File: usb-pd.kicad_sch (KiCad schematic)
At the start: 71 parts, among them J3 USB-C_GCT_USB4105-GF-A, J4 JST_SH_1x4_SM04B-SRSS-TB-LF-SN, Q4 SQS401EN-T1_BE3, U2 TVS2200DRVR, U6 STUSB4500_QFN, U9 SIC477ED-T1-GE3

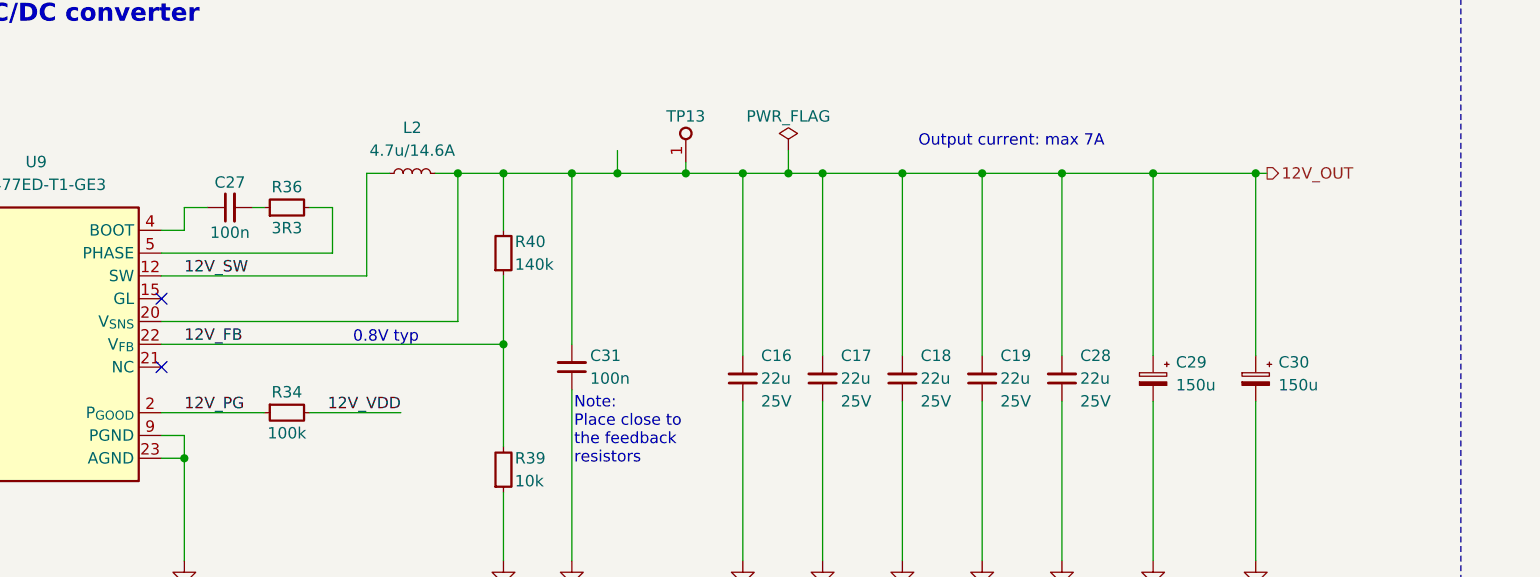
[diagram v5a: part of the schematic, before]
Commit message: [#79262] Remove 12V DC-DC R_boot resistor
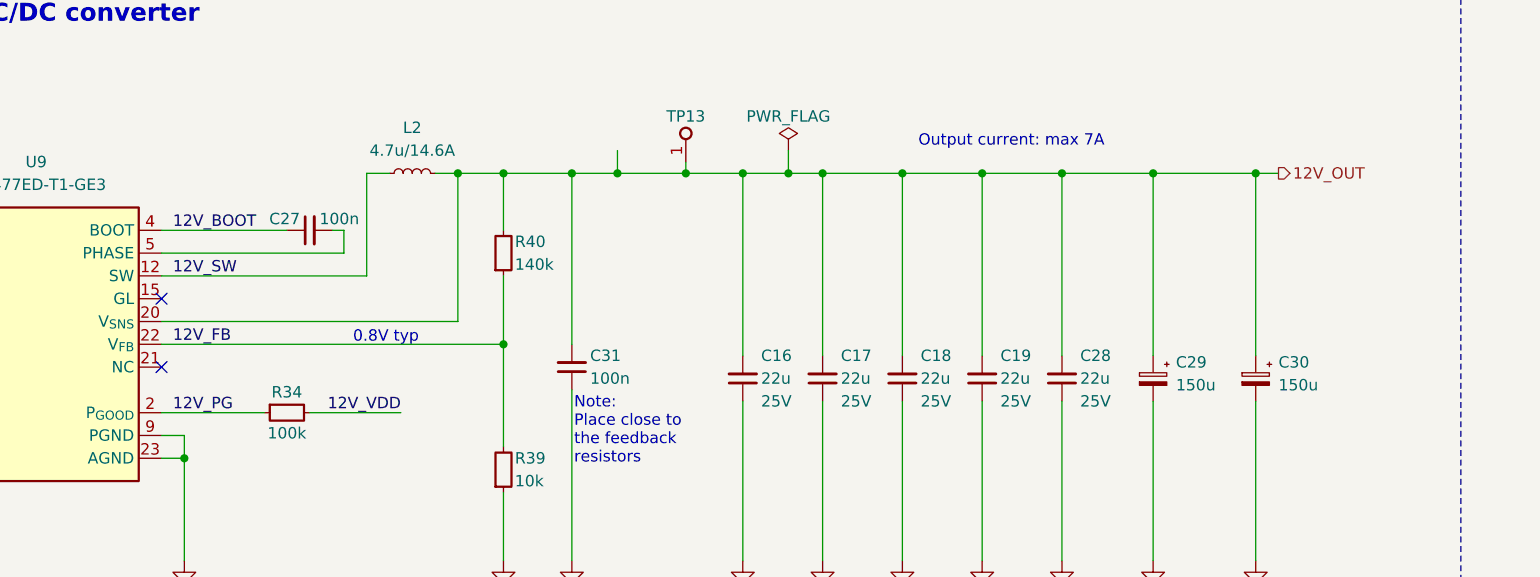
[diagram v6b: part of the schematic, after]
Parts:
- removed R36: R_3R3_0402, antmicro-footprints:R_0402_1005Metric, symbol antmicroResistors0402:R_3R3_0402
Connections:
- net 12V_BOOT: now reaches C27.1, U9.4 (BOOT)
- net at C27.2: now also U9.5 (PHASE), U9.6 (PHASE)
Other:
- moved on the sheet: C27
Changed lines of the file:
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@@
 	(wire
 		(pts
-			(xy 144.78 203.2) (xy 163.83 203.2)
+			(xy 144.78 203.2) (xy 165.1 203.2)
 		)
 		(stroke
@@
 	(wire
 		(pts
-			(xy 147.32 198.12) (xy 147.32 200.66)
-		)
-		(stroke
-			(width 0)
-			(type default)
-		)
-	)
-	(wire
-		(pts
 			(xy 233.68 107.95) (xy 233.68 111.76)
 		)
@@
 		)
 	)
+	(wire
+		(pts
+			(xy 165.1 200.66) (xy 163.83 200.66)
+		)
+		(stroke
+			(width 0)
+			(type default)
+		)
+	)
 	(polyline
 		(pts
@@
 	(wire
 		(pts
-			(xy 163.83 198.12) (xy 161.29 198.12)
-		)
-		(stroke
-			(width 0)
-			(type default)
-		)
-	)
-	(wire
-		(pts
 			(xy 233.68 99.06) (xy 233.68 102.87)
 		)
@@
 	(wire
 		(pts
-			(xy 163.83 203.2) (xy 163.83 198.12)
+			(xy 165.1 203.2) (xy 165.1 200.66)
 		)
 		(stroke
@@
 	(wire
 		(pts
-			(xy 154.94 198.12) (xy 156.21 198.12)
-		)
-		(stroke
-			(width 0)
-			(type default)
-		)
-	)
-	(wire
-		(pts
 			(xy 74.93 201.93) (xy 74.93 203.2)
 		)
@@
 	(wire
 		(pts
-			(xy 147.32 198.12) (xy 149.86 198.12)
-		)
-		(stroke
-			(width 0)
-			(type default)
-		)
-	)
-	(wire
-		(pts
 			(xy 190.5 194.31) (xy 190.5 213.36)
 		)
@@
 	(wire
 		(pts
-			(xy 144.78 200.66) (xy 147.32 200.66)
+			(xy 144.78 200.66) (xy 158.75 200.66)
 		)
 		(stroke
@@
 	(wire
 		(pts
-			(xy 267.97 194.31) (xy 266.7 194.31)
+			(xy 269.24 194.31) (xy 266.7 194.31)
 		)
 		(stroke
@@
 	)
 	(label "12V_SW"
-		(at 147.32 205.74 0)
+		(at 146.05 205.74 0)
 		(effects
 			(font
@@
 		)
 	)
+	(label "12V_BOOT"
+		(at 146.05 200.66 0)
+		(effects
+			(font
+				(size 1.27 1.27)
+			)
+			(justify left bottom)
+		)
+	)
 	(label "SCL"
 		(at 393.7 88.9 180)
@@
 	)
 	(label "12V_FB"
-		(at 147.32 213.36 0)
+		(at 146.05 213.36 0)
 		(effects
 			(font
@@
 	)
 	(label "12V_PG"
-		(at 147.32 220.98 0)
+		(at 146.05 220.98 0)
 		(effects
 			(font
@@
 	(hierarchical_label "12V_OUT"
 		(shape output)
-		(at 267.97 194.31 0)
+		(at 269.24 194.31 0)
 		(effects
 			(font
@@
 	(symbol
 		(lib_id "antmicroCapacitors0402:C_100n_0402")
-		(at 149.86 198.12 0)
+		(at 158.75 200.66 0)
 		(unit 1)
 		(exclude_from_sim no)
@@
 		(dnp no)
 		(property "Reference" "C27"
-			(at 152.4 195.326 0)
+			(at 158.496 199.39 0)
 			(effects
 				(font
@@
 		)
 		(property "Value" "C_100n_0402"
-			(at 170.18 208.28 0)
+			(at 179.07 210.82 0)
 			(effects
 				(font
@@
 		)
 		(property "Footprint" "antmicro-footprints:C_0402_1005Metric"
-			(at 170.18 210.82 0)
+			(at 179.07 213.36 0)
 			(effects
 				(font
@@
 		)
 		(property "Datasheet" "https://www.murata.com/products/productdetail?partno=GRM155R61H104KE14%23"
-			(at 170.18 213.36 0)
+			(at 179.07 215.9 0)
 			(effects
 				(font
@@
 		)
 		(property "Description" "SMD Multilayer Ceramic Capacitor, 0.1 µF, 50 V, 0402 [1005 Metric], ± 10%, X5R, GRM Series"
-			(at 149.86 198.12 0)
+			(at 158.75 200.66 0)
 			(effects
 				(font
@@
 		)
 		(property "MPN" "GRM155R61H104KE14D"
-			(at 170.18 215.9 0)
+			(at 179.07 218.44 0)
 			(effects
 				(font
@@
 		)
 		(property "Manufacturer" "Murata"
-			(at 170.18 218.44 0)
+			(at 179.07 220.98 0)
 			(effects
 				(font
@@
 		)
 		(property "License" "Apache-2.0"
-			(at 170.18 220.98 0)
+			(at 179.07 223.52 0)
 			(effects
 				(font
@@
 		)
 		(property "Author" "Antmicro"
-			(at 170.18 223.52 0)
+			(at 179.07 226.06 0)
 			(effects
 				(font
@@
 		)
 		(property "Val" "100n"
-			(at 152.4 200.914 0)
+			(at 164.592 199.39 0)
 			(effects
 				(font
@@
 		)
 		(property "Voltage" "50V"
-			(at 170.18 226.06 0)
+			(at 179.07 228.6 0)
 			(effects
 				(font
@@
 		)
 		(property "Dielectric" "X5R"
-			(at 170.18 228.6 0)
+			(at 179.07 231.14 0)
 			(effects
 				(font
@@
 					(unit 1)
 				)
-			)
-		)
-	)
-	(symbol
-		(lib_id "antmicroResistors0402:R_3R3_0402")
-		(at 156.21 198.12 0)
-		(mirror x)
-		(unit 1)
-		(exclude_from_sim no)
-		(in_bom yes)
-		(on_board yes)
-		(dnp no)
-		(property "Reference" "R36"
-			(at 158.75 195.834 0)
-			(effects
-				(font
-					(size 1.27 1.27)
-				)
-			)
-		)
-		(property "Value" "R_3R3_0402"
-			(at 156.21 194.31 0)
-			(effects
-				(font
-					(size 1.27 1.27)
-				)
-				(justify left)
-				(hide yes)
-			)
-		)
-		(property "Footprint" "antmicro-footprints:R_0402_1005Metric"
-			(at 161.29 203.2 0)
-			(effects
-				(font
-					(size 1.27 1.27)
-					(thickness 0.15)
-				)
-				(justify left bottom)
-				(hide yes)
-			)
-		)
-		(property "Datasheet" "https://www.bourns.com/docs/product-datasheets/cr.pdf"
-			(at 156.21 198.12 0)
-			(effects
-				(font
-					(size 1.27 1.27)
-					(thickness 0.15)
-				)
-				(justify left bottom)
-				(hide yes)
-			)
-		)
-		(property "Description" "SMD Chip Resistor, 3.3 ohm, ± 1%, 62.5 mW, 0402 [1005 Metric], Thick Film, General Purpose"
-			(at 156.21 198.12 0)
-			(effects
-				(font
-					(size 1.27 1.27)
-				)
-				(hide yes)
-			)
-		)
-		(property "Manufacturer" "Bourns"
-			(at 161.29 208.28 0)
-			(effects
-				(font
-					(size 1.27 1.27)
-					(thickness 0.15)
-				)
-				(justify left bottom)
-				(hide yes)
-			)
-		)
-		(property "MPN" "CR0402-FX-3R30GLF"
-			(at 161.29 205.74 0)
-			(effects
-				(font
-					(size 1.27 1.27)
-					(thickness 0.15)
-				)
-				(justify left bottom)
-				(hide yes)
-			)
-		)
-		(property "Val" "3R3"
-			(at 158.75 200.406 0)
-			(effects
-				(font
-					(size 1.27 1.27)
-					(thickness 0.15)
-				)
-			)
-		)
-		(property "License" "Apache-2.0"
-			(at 176.53 172.72 0)
-			(effects
-				(font
-					(size 1.27 1.27)
-					(thickness 0.15)
-				)
-				(justify left bottom)
-				(hide yes)
-			)
-		)
-		(property "Author" "Antmicro"
-			(at 176.53 170.18 0)
-			(effects
-				(font
-					(size 1.27 1.27)
-					(thickness 0.15)
-				)
-				(justify left bottom)
-				(hide yes)
-			)
-		)
-		(property "Tolerance" "1%"
-			(at 176.53 187.96 0)
-			(effects
-				(font
-					(size 1.27 1.27)
-				)
-				(justify left bottom)
-				(hide yes)
-			)
-		)
-		(pin "1"
-		)
-		(pin "2"
-		)
-		(instances
-			(project "oculink-to-pcie-adapter"
-				(path "/44c3be85-0a18-4d93-a9a5-650ee09b6032/967dc2ce-6faa-4f65-adf2-eb5d333aef74"
-					(reference "R36")
-					(unit 1)
-				)

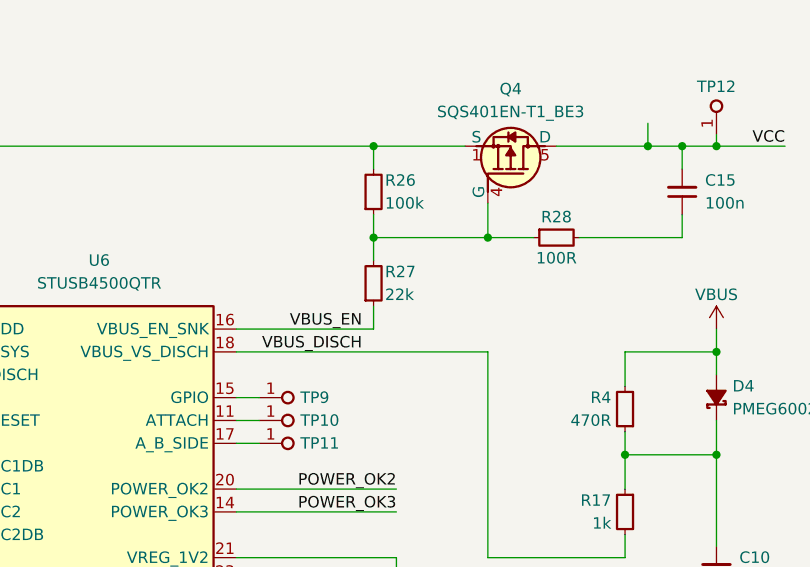
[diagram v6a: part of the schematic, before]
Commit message: [#79262] Reduce Q4 max Vgs
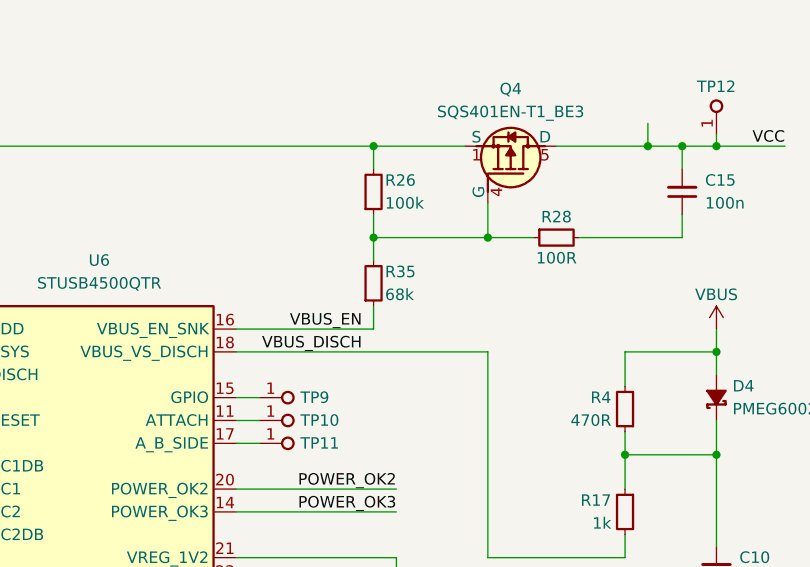
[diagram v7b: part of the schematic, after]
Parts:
- removed R27: R_22k_0402, antmicro-footprints:R_0402_1005Metric, symbol antmicroResistors0402:R_22k_0402
- added R35: R_68k_0402, antmicro-footprints:R_0402_1005Metric, symbol antmicroResistors0402:R_68k_0402
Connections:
- net VBUS_EN: now also R35.1
- net at Q4.4 (G), R26.1, R28.1: now also R35.2
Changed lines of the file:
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@@
 	)
 	(symbol
+		(lib_id "antmicroResistors0402:R_68k_0402")
+		(at 240.03 68.58 90)
+		(unit 1)
+		(exclude_from_sim no)
+		(in_bom yes)
+		(on_board yes)
+		(dnp no)
+		(property "Reference" "R35"
+			(at 241.3 64.77 90)
+			(effects
+				(font
+					(size 1.27 1.27)
+					(thickness 0.15)
+				)
+				(justify right)
+			)
+		)
+		(property "Value" "R_68k_0402"
+			(at 252.73 48.26 0)
+			(effects
+				(font
+					(size 1.27 1.27)
+					(thickness 0.15)
+				)
+				(justify left bottom)
+				(hide yes)
+			)
+		)
+		(property "Footprint" "antmicro-footprints:R_0402_1005Metric"
+			(at 255.27 48.26 0)
+			(effects
+				(font
+					(size 1.27 1.27)
+					(thickness 0.15)
+				)
+				(justify left bottom)
+				(hide yes)
+			)
+		)
+		(property "Datasheet" "https://www.bourns.com/docs/product-datasheets/cr.pdf"
+			(at 257.81 48.26 0)
+			(effects
+				(font
+					(size 1.27 1.27)
+					(thickness 0.15)
+				)
+				(justify left bottom)
+				(hide yes)
+			)
+		)
+		(property "Description" "SMD Chip Resistor"
+			(at 240.03 68.58 0)
+			(effects
+				(font
+					(size 1.27 1.27)
+				)
+				(hide yes)
+			)
+		)
+		(property "MPN" "CR0402-FX-6802GLF"
+			(at 260.35 48.26 0)
+			(effects
+				(font
+					(size 1.27 1.27)
+					(thickness 0.15)
+				)
+				(justify left bottom)
+				(hide yes)
+			)
+		)
+		(property "Manufacturer" "Bourns"
+			(at 262.89 48.26 0)
+			(effects
+				(font
+					(size 1.27 1.27)
+					(thickness 0.15)
+				)
+				(justify left bottom)
+				(hide yes)
+			)
+		)
+		(property "License" "Apache-2.0"
+			(at 265.43 48.26 0)
+			(effects
+				(font
+					(size 1.27 1.27)
+					(thickness 0.15)
+				)
+				(justify left bottom)
+				(hide yes)
+			)
+		)
+		(property "Author" "Antmicro"
+			(at 267.97 48.26 0)
+			(effects
+				(font
+					(size 1.27 1.27)
+					(thickness 0.15)
+				)
+				(justify left bottom)
+				(hide yes)
+			)
+		)
+		(property "Val" "68k"
+			(at 241.3 67.31 90)
+			(effects
+				(font
+					(size 1.27 1.27)
+					(thickness 0.15)
+				)
+				(justify right)
+			)
+		)
+		(property "Tolerance" "1%"
+			(at 250.19 48.26 0)
+			(effects
+				(font
+					(size 1.27 1.27)
+				)
+				(justify left bottom)
+				(hide yes)
+			)
+		)
+		(pin "2"
+		)
+		(pin "1"
+		)
+		(instances
+			(project ""
+				(path "/44c3be85-0a18-4d93-a9a5-650ee09b6032/967dc2ce-6faa-4f65-adf2-eb5d333aef74"
+					(reference "R35")
+					(unit 1)
+				)
+			)
+		)
+	)
+	(symbol
 		(lib_id "antmicroPMICPowerDistributionSwitchesLoadDrivers:STUSB4500_QFN")
 		(at 194.31 71.12 0)
@@
 					(unit 1)
 				)
-			)
-		)
-	)
-	(symbol
-		(lib_id "antmicroResistors0402:R_22k_0402")
-		(at 240.03 68.58 90)
-		(unit 1)
-		(exclude_from_sim no)
-		(in_bom yes)
-		(on_board yes)
-		(dnp no)
-		(property "Reference" "R27"
-			(at 241.3 64.77 90)
-			(effects
-				(font
-					(size 1.27 1.27)
-					(thickness 0.15)
-				)
-				(justify right)
-			)
-		)
-		(property "Value" "R_22k_0402"
-			(at 252.73 48.26 0)
-			(effects
-				(font
-					(size 1.27 1.27)
-					(thickness 0.15)
-				)
-				(justify left bottom)
-				(hide yes)
-			)
-		)
-		(property "Footprint" "antmicro-footprints:R_0402_1005Metric"
-			(at 255.27 48.26 0)
-			(effects
-				(font
-					(size 1.27 1.27)
-					(thickness 0.15)
-				)
-				(justify left bottom)
-				(hide yes)
-			)
-		)
-		(property "Datasheet" "https://www.bourns.com/docs/product-datasheets/cr.pdf"
-			(at 257.81 48.26 0)
-			(effects
-				(font
-					(size 1.27 1.27)
-					(thickness 0.15)
-				)
-				(justify left bottom)
-				(hide yes)
-			)
-		)
-		(property "Description" "SMD Chip Resistor, 22 kohm, ± 1%, 62.5 mW, 0402 [1005 Metric], Thick Film, General Purpose"
-			(at 240.03 68.58 0)
-			(effects
-				(font
-					(size 1.27 1.27)
-				)
-				(hide yes)
-			)
-		)
-		(property "MPN" "CR0402-FX-2202GLF"
-			(at 260.35 48.26 0)
-			(effects
-				(font
-					(size 1.27 1.27)
-					(thickness 0.15)
-				)
-				(justify left bottom)
-				(hide yes)
-			)
-		)
-		(property "Manufacturer" "Bourns"
-			(at 262.89 48.26 0)
-			(effects
-				(font
-					(size 1.27 1.27)
-					(thickness 0.15)
-				)
-				(justify left bottom)
-				(hide yes)
-			)
-		)
-		(property "License" "Apache-2.0"
-			(at 265.43 48.26 0)
-			(effects
-				(font
-					(size 1.27 1.27)
-					(thickness 0.15)
-				)
-				(justify left bottom)
-				(hide yes)
-			)
-		)
-		(property "Author" "Antmicro"
-			(at 267.97 48.26 0)
-			(effects
-				(font
-					(size 1.27 1.27)
-					(thickness 0.15)
-				)
-				(justify left bottom)
-				(hide yes)
-			)
-		)
-		(property "Val" "22k"
-			(at 241.3 67.31 90)
-			(effects
-				(font
-					(size 1.27 1.27)
-					(thickness 0.15)
-				)
-				(justify right)
-			)
-		)
-		(property "Tolerance" "1%"
-			(at 250.19 48.26 0)
-			(effects
-				(font
-					(size 1.27 1.27)
-				)
-				(justify left bottom)
-				(hide yes)
-			)
-		)
-		(pin "1"
-		)
-		(pin "2"
-		)
-		(instances
-			(project "oculink-to-pcie-adapter"
-				(path "/44c3be85-0a18-4d93-a9a5-650ee09b6032/967dc2ce-6faa-4f65-adf2-eb5d333aef74"
-					(reference "R27")
-					(unit 1)
-				)

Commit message: [#79262] Change USB PD controller to CYPD3177
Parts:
- removed C10: C_10u_0805_35V, antmicro-footprints:C_0805_2012Metric, symbol antmicroCapacitorsmisc:C_10u_0805_35V
- removed C11, C15: C_100n_0402, antmicro-footprints:C_0402_1005Metric, symbol antmicroCapacitors0402:C_100n_0402
- removed C12, C13, C14: C_1u_25V_0402, antmicro-footprints:C_0402_1005Metric, symbol antmicroCapacitors0402:C_1u_25V_0402
- removed D18: ESD204DQAR, antmicro-footprints:USON-10_2.5x1mm_P0.5mm, symbol antmicroTVSDiodes:ESD204DQAR
- removed D4: PMEG6002EJ,115, antmicro-footprints:D_SOD-323F, symbol antmicroDiodesRectifiersSingle:PMEG6002EJ,115
- removed D6, D7: LED_G_0603_LTST-C190GKT, antmicro-footprints:LED_0603_1608Metric_G, symbol antmicroLEDIndicationDiscrete:LED_G_0603_LTST-C190GKT
- removed J4: JST_SH_1x4_SM04B-SRSS-TB-LF-SN, antmicro-footprints:Conn_JST_SH_1x4_SM04B-SRSS-TB-LF-SN, symbol antmicroWire2BoardConnectors:JST_SH_1x4_SM04B-SRSS-TB-LF-SN
- removed Q4: SQS401EN-T1_BE3, antmicro-footprints:Vishay_PowerPAK_1212-8_Single, symbol antmicroTransistorsFETsMOSFETsSingle:SQS401EN-T1_BE3
- removed R17, R24, R25: R_1k_0402, antmicro-footprints:R_0402_1005Metric, symbol antmicroResistors0402:R_1k_0402
- removed R18: R_0R_0402, antmicro-footprints:R_0402_1005Metric, symbol antmicroResistors0402:R_0R_0402
- removed R19, R20, R22: R_4k7_0402, antmicro-footprints:R_0402_1005Metric, symbol antmicroResistors0402:R_4k7_0402
- removed R26: R_100k_0402, antmicro-footprints:R_0402_1005Metric, symbol antmicroResistors0402:R_100k_0402
- removed R28: R_100R_0402, antmicro-footprints:R_0402_1005Metric, symbol antmicroResistors0402:R_100R_0402
- removed R35: R_68k_0402, antmicro-footprints:R_0402_1005Metric, symbol antmicroResistors0402:R_68k_0402
- removed R4: R_470R_0402, antmicro-footprints:R_0402_1005Metric, symbol antmicroResistors0402:R_470R_0402
- removed TP10, TP11, TP12, TP7, TP8, TP9: TP_0.75mm_SMD, antmicro-footprints:TP_SMD_0.75mm, symbol antmicroTestPoints:TP_0.75mm_SMD
- removed U2: TVS2200DRVR, antmicro-footprints:WSON-6-1EP_2x2mm_P0.65mm, symbol antmicroTVSDiodes:TVS2200DRVR
- removed U6: STUSB4500_QFN, antmicro-footprints:QFN-24-1EP_4x4mm_P0.5_EP2.1x2.1mm, symbol antmicroPMICPowerDistributionSwitchesLoadDrivers:STUSB4500_QFN
- added C11, C38, C39: C_1u_25V_0402, antmicro-footprints:C_0402_1005Metric, symbol antmicroCapacitors0402:C_1u_25V_0402
- added C40, C41: C_100n_0402, antmicro-footprints:C_0402_1005Metric, symbol antmicroCapacitors0402:C_100n_0402
- added D18: LED_G_0603_LTST-C190GKT, antmicro-footprints:LED_0603_1608Metric_G, symbol antmicroLEDIndicationDiscrete:LED_G_0603_LTST-C190GKT
- added D19: BZT52B15SV-T, antmicro-footprints:D_SOD-323, symbol antmicroDiodesZenerSingle:BZT52B15SV-T
- added D21: ESDA25P35-1U1M, antmicro-footprints:QFN-2L_1.6x1x0.55mm, symbol antmicroTVSDiodes:ESDA25P35-1U1M
- added Q6: SQS401EN-T1_BE3, antmicro-footprints:Vishay_PowerPAK_1212-8_Single, symbol antmicroTransistorsFETsMOSFETsSingle:SQS401EN-T1_BE3
- added Q8: BSS138-7-F, antmicro-footprints:SOT-23-3, symbol antmicroTransistorsFETsMOSFETsSingle:BSS138-7-F
- added R17, R22, R24, R25, R26, R27, R28, R38, R4, R41: R_10k_0402, antmicro-footprints:R_0402_1005Metric, symbol antmicroResistors0402:R_10k_0402
- added R18, R19: R_2k_0402, antmicro-footprints:R_0402_1005Metric, symbol antmicroResistors0402:R_2k_0402
- added R20: R_49k9_0402, antmicro-footprints:R_0402_1005Metric, symbol antmicroResistors0402:R_49k9_0402
- added R37: R_1k_0402, antmicro-footprints:R_0402_1005Metric, symbol antmicroResistors0402:R_1k_0402
- added TP14: TP_0.75mm_SMD, antmicro-footprints:TP_SMD_0.75mm, symbol antmicroTestPoints:TP_0.75mm_SMD
- added U5: CYPD3177-24LQXQ, antmicro-footprints:QFN-24-1EP_4x4mm_P0.5mm_EP2.6x2.6mm, symbol antmicroInterfaceControllers:CYPD3177-24LQXQ
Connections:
- net CC1: now also U5.15 (CC1)
- net CC2: now also U5.14 (CC2)
- net GND: now also C11.1, C39.1, C40.1, C41.1, D21.2 (A), Q8.2 (S), R17.1, R22.1, R25.1, R28.1, R38.1, U5.19 (GND), U5.22 (GND), U5.25 (GND); no longer R21.2
- net SCL: now also R18.1, U5.13 (HPI_SCL); no longer TP6.1
- net SDA: now also R19.1, U5.12 (HPI_SDA); no longer TP5.1
- net VBUS: now also D19.1 (C), D21.1 (C), Q6.1 (S), Q6.2 (S), Q6.3 (S), R27.2, R41.2, U5.18 (VBUS_IN)
- net VBUS_EN: now also R37.1, U5.3 (VBUS_FET_EN)
- net VCC: now also C38.2, Q6.5 (D), TP14.1, U5.11 (VDC_OUT)
- net VBUS_MAX: now reaches R21.1
- net VBUS_MAX: now also R22.2, U5.2 (VBUS_MAX)
- new net: C38.1, D19.2 (A), Q6.4 (G), R27.1, R37.2
- new net: D18.2 (A), R41.1
- new net: D18.1 (C), Q8.3 (D)
- new net FAULT: Q8.1 (G), R38.2, U5.9 (FAULT)
- new net FLIP: R20.1, U5.10 (FLIP)
- new net GPIO_1: TP6.1, U5.8 (GPIO_1)
- new net ISNK_COARSE: R26.1, R28.2, U5.5 (ISNK_COARSE)
- new net ISNK_FINE: R24.1, R25.2, U5.6 (ISNK_FINE)
- new net VBUS_MIN: R17.2, R4.1, U5.1 (VBUS_MIN)
- new net VCCD_1V8: C11.2, U5.24 (VCCD)
- new net VDDD_3V3: C39.2, C40.2, C41.2, R18.2, R19.2, R20.2, R21.2, R24.2, R26.2, R4.2, U5.23 (VDDD)
- new net ~{HPI_INT}: TP5.1, U5.7 (~{HPI_INT})
- no-connect marks 10 -> 14
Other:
- note added: "50kΩ sets the UFP VDO data capability bit is set to 0"
- note removed: "LED Indicators"
- note removed: "QWIIC I2C Connector"
- moved on the sheet: C16, C17, C18, C19, C20, C21, C22, C23, C24, C25, C26, C27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
